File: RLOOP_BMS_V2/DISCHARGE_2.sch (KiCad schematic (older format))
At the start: 60 parts, among them Q10 PMV20ENR, Q11 PMV20ENR, Q12 PMV20ENR, Q13 PMV20ENR, Q8 PMV20ENR, Q9 PMV20ENR

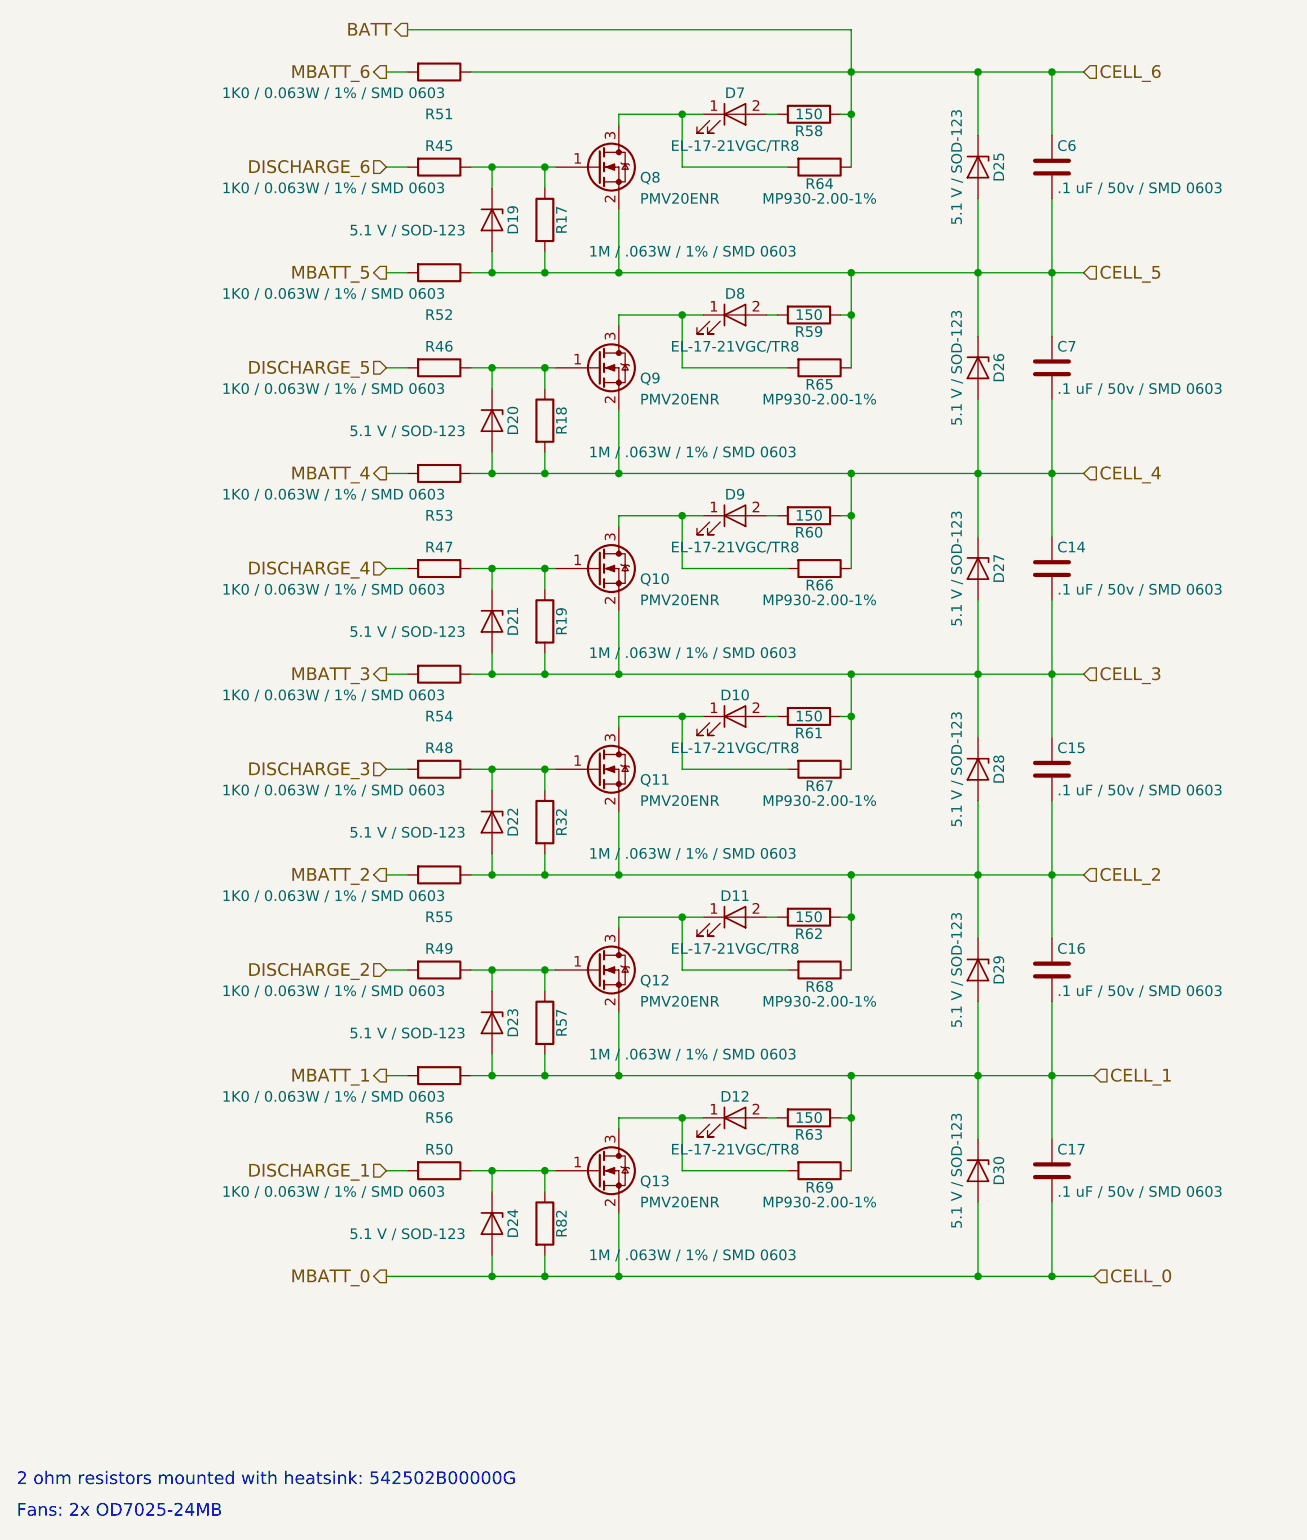
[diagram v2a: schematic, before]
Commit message: Added BOM, added pin 1 markings on a few parts
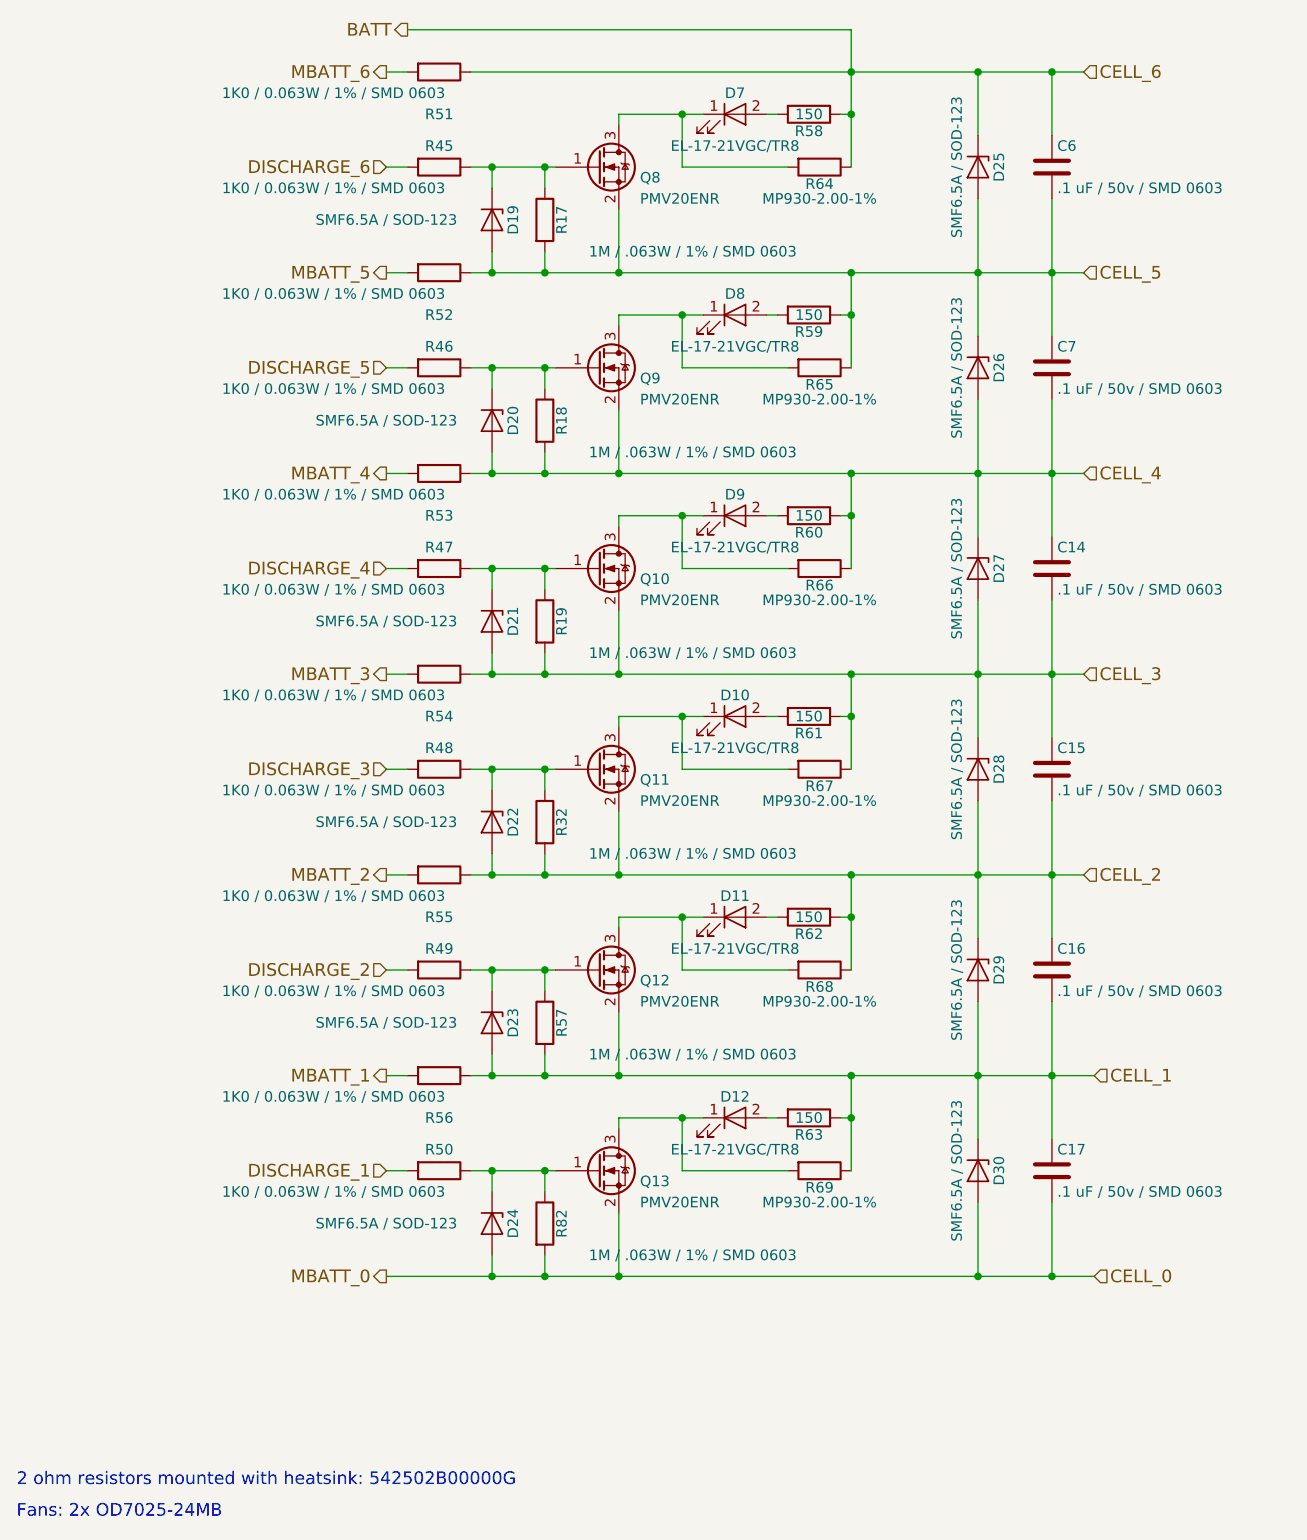
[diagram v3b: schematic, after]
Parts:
- D19, D20, D21, D22, D23, D24, D25, D26, D27, D28, D29, D30: value 5.1 V / SOD-123 -> SMF6.5A / SOD-123
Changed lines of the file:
@@
 P 6750 1300
 F 0 "D25" H 6750 1400 50  0000 C CNN
-F 1 "5.1 V / SOD-123" H 6750 1200 50  0000 C CNN
+F 1 "SMF6.5A / SOD-123" H 6750 1200 50  0000 C CNN
 F 2 "Diodes_SMD:D_SOD-123" H 6750 1300 50  0001 C CNN
 F 3 "" H 6750 1300 50  0001 C CNN
@@
 P 6750 2250
 F 0 "D26" H 6750 2350 50  0000 C CNN
-F 1 "5.1 V / SOD-123" H 6750 2150 50  0000 C CNN
+F 1 "SMF6.5A / SOD-123" H 6750 2150 50  0000 C CNN
 F 2 "Diodes_SMD:D_SOD-123" H 6750 2250 50  0001 C CNN
 F 3 "" H 6750 2250 50  0001 C CNN
@@
 P 6750 3200
 F 0 "D27" H 6750 3300 50  0000 C CNN
-F 1 "5.1 V / SOD-123" H 6750 3100 50  0000 C CNN
+F 1 "SMF6.5A / SOD-123" H 6750 3100 50  0000 C CNN
 F 2 "Diodes_SMD:D_SOD-123" H 6750 3200 50  0001 C CNN
 F 3 "" H 6750 3200 50  0001 C CNN
@@
 P 6750 4150
 F 0 "D28" H 6750 4250 50  0000 C CNN
-F 1 "5.1 V / SOD-123" H 6750 4050 50  0000 C CNN
+F 1 "SMF6.5A / SOD-123" H 6750 4050 50  0000 C CNN
 F 2 "Diodes_SMD:D_SOD-123" H 6750 4150 50  0001 C CNN
 F 3 "" H 6750 4150 50  0001 C CNN
@@
 P 6750 5100
 F 0 "D29" H 6750 5200 50  0000 C CNN
-F 1 "5.1 V / SOD-123" H 6750 5000 50  0000 C CNN
+F 1 "SMF6.5A / SOD-123" H 6750 5000 50  0000 C CNN
 F 2 "Diodes_SMD:D_SOD-123" H 6750 5100 50  0001 C CNN
 F 3 "" H 6750 5100 50  0001 C CNN
@@
 P 6750 6050
 F 0 "D30" H 6750 6150 50  0000 C CNN
-F 1 "5.1 V / SOD-123" H 6750 5950 50  0000 C CNN
+F 1 "SMF6.5A / SOD-123" H 6750 5950 50  0000 C CNN
 F 2 "Diodes_SMD:D_SOD-123" H 6750 6050 50  0001 C CNN
 F 3 "" H 6750 6050 50  0001 C CNN
@@
 P 4450 1550
 F 0 "D19" H 4450 1650 50  0000 C CNN
-F 1 "5.1 V / SOD-123" V 4500 1150 50  0000 C CNN
+F 1 "SMF6.5A / SOD-123" V 4450 1050 50  0000 C CNN
 F 2 "Diodes_SMD:D_SOD-123" H 4450 1550 50  0001 C CNN
 F 3 "" H 4450 1550 50  0001 C CNN
@@
 P 4450 2500
 F 0 "D20" H 4450 2600 50  0000 C CNN
-F 1 "5.1 V / SOD-123" V 4500 2100 50  0000 C CNN
+F 1 "SMF6.5A / SOD-123" V 4450 2000 50  0000 C CNN
 F 2 "Diodes_SMD:D_SOD-123" H 4450 2500 50  0001 C CNN
 F 3 "" H 4450 2500 50  0001 C CNN
@@
 P 4450 3450
 F 0 "D21" H 4450 3550 50  0000 C CNN
-F 1 "5.1 V / SOD-123" V 4500 3050 50  0000 C CNN
+F 1 "SMF6.5A / SOD-123" V 4450 2950 50  0000 C CNN
 F 2 "Diodes_SMD:D_SOD-123" H 4450 3450 50  0001 C CNN
 F 3 "" H 4450 3450 50  0001 C CNN
@@
 P 4450 4400
 F 0 "D22" H 4450 4500 50  0000 C CNN
-F 1 "5.1 V / SOD-123" V 4500 4000 50  0000 C CNN
+F 1 "SMF6.5A / SOD-123" V 4450 3900 50  0000 C CNN
 F 2 "Diodes_SMD:D_SOD-123" H 4450 4400 50  0001 C CNN
 F 3 "" H 4450 4400 50  0001 C CNN
@@
 P 4450 5350
 F 0 "D23" H 4450 5450 50  0000 C CNN
-F 1 "5.1 V / SOD-123" V 4500 4950 50  0000 C CNN
+F 1 "SMF6.5A / SOD-123" V 4450 4850 50  0000 C CNN
 F 2 "Diodes_SMD:D_SOD-123" H 4450 5350 50  0001 C CNN
 F 3 "" H 4450 5350 50  0001 C CNN
@@
 P 4450 6300
 F 0 "D24" H 4450 6400 50  0000 C CNN
-F 1 "5.1 V / SOD-123" V 4500 5900 50  0000 C CNN
+F 1 "SMF6.5A / SOD-123" V 4450 5800 50  0000 C CNN
 F 2 "Diodes_SMD:D_SOD-123" H 4450 6300 50  0001 C CNN
 F 3 "" H 4450 6300 50  0001 C CNN

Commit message: swapped a few connectors to standardize with the power node and what's readily available
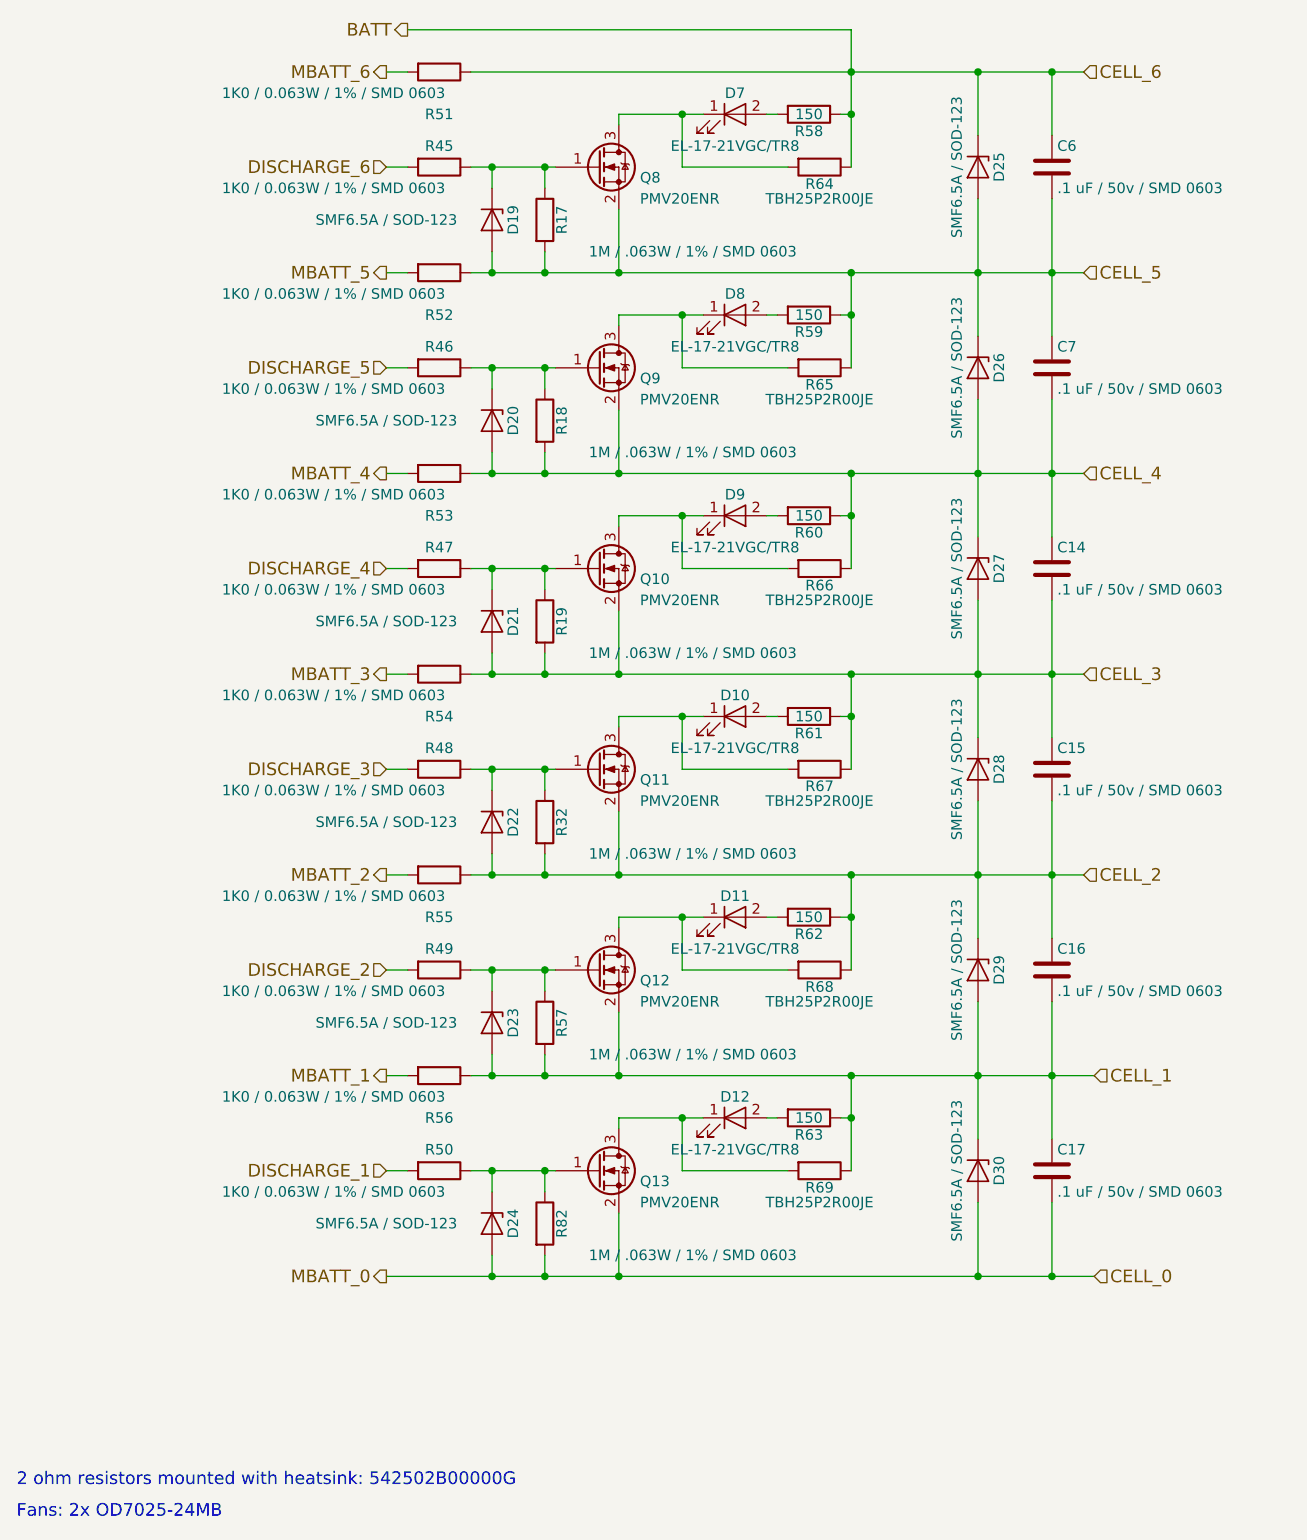
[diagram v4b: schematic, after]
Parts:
- R64, R65, R66, R67, R68, R69: value MP930-2.00-1% -> TBH25P2R00JE; footprint rLoop_Footprints:Res_MP930 -> rLoop_Footprints:2-OHM-TO-220-TBH25P2R00JE
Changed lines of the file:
@@
 P 6000 1300
 F 0 "R64" V 6080 1300 50  0000 C CNN
-F 1 "MP930-2.00-1%" V 6150 1300 50  0000 C CNN
-F 2 "rLoop_Footprints:Res_MP930" V 5930 1300 50  0001 C CNN
+F 1 "TBH25P2R00JE" V 6150 1300 50  0000 C CNN
+F 2 "rLoop_Footprints:2-OHM-TO-220-TBH25P2R00JE" V 5930 1300 50  0001 C CNN
 F 3 "" H 6000 1300 50  0001 C CNN
 	1    6000 1300
@@
 P 6000 2250
 F 0 "R65" V 6080 2250 50  0000 C CNN
-F 1 "MP930-2.00-1%" V 6150 2250 50  0000 C CNN
-F 2 "rLoop_Footprints:Res_MP930" V 5930 2250 50  0001 C CNN
+F 1 "TBH25P2R00JE" V 6150 2250 50  0000 C CNN
+F 2 "rLoop_Footprints:2-OHM-TO-220-TBH25P2R00JE" V 5930 2250 50  0001 C CNN
 F 3 "" H 6000 2250 50  0001 C CNN
 	1    6000 2250
@@
 P 6000 3200
 F 0 "R66" V 6080 3200 50  0000 C CNN
-F 1 "MP930-2.00-1%" V 6150 3200 50  0000 C CNN
-F 2 "rLoop_Footprints:Res_MP930" V 5930 3200 50  0001 C CNN
+F 1 "TBH25P2R00JE" V 6150 3200 50  0000 C CNN
+F 2 "rLoop_Footprints:2-OHM-TO-220-TBH25P2R00JE" V 5930 3200 50  0001 C CNN
 F 3 "" H 6000 3200 50  0001 C CNN
 	1    6000 3200
@@
 P 6000 4150
 F 0 "R67" V 6080 4150 50  0000 C CNN
-F 1 "MP930-2.00-1%" V 6150 4150 50  0000 C CNN
-F 2 "rLoop_Footprints:Res_MP930" V 5930 4150 50  0001 C CNN
+F 1 "TBH25P2R00JE" V 6150 4150 50  0000 C CNN
+F 2 "rLoop_Footprints:2-OHM-TO-220-TBH25P2R00JE" V 5930 4150 50  0001 C CNN
 F 3 "" H 6000 4150 50  0001 C CNN
 	1    6000 4150
@@
 P 6000 5100
 F 0 "R68" V 6080 5100 50  0000 C CNN
-F 1 "MP930-2.00-1%" V 6150 5100 50  0000 C CNN
-F 2 "rLoop_Footprints:Res_MP930" V 5930 5100 50  0001 C CNN
+F 1 "TBH25P2R00JE" V 6150 5100 50  0000 C CNN
+F 2 "rLoop_Footprints:2-OHM-TO-220-TBH25P2R00JE" V 5930 5100 50  0001 C CNN
 F 3 "" H 6000 5100 50  0001 C CNN
 	1    6000 5100
@@
 P 6000 6050
 F 0 "R69" V 6080 6050 50  0000 C CNN
-F 1 "MP930-2.00-1%" V 6150 6050 50  0000 C CNN
-F 2 "rLoop_Footprints:Res_MP930" V 5930 6050 50  0001 C CNN
+F 1 "TBH25P2R00JE" V 6150 6050 50  0000 C CNN
+F 2 "rLoop_Footprints:2-OHM-TO-220-TBH25P2R00JE" V 5930 6050 50  0001 C CNN
 F 3 "" H 6000 6050 50  0001 C CNN
 	1    6000 6050
